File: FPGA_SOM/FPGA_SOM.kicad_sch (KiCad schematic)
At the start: 95 parts, among them J1 Conn_02x06_Top_Bottom, J1 USB_C_Receptacle_USB2.0, J10 Conn_01x06, J2 Conn_02x05_Counter_Clockwise, J5 Conn_01x02, J6 Conn_01x06, J9 RJ45_Bel_SI-60062-F, SW1 SW_Push, U1 ICE40UP5K-SG48ITR, U101 W25Q128JVSIQ, U2 AP2127N-3.3, U3 AP2127N-1.2, U6 LAN8720A, X101 SX2M20.000B10F20TNN, Y1 25 MHz

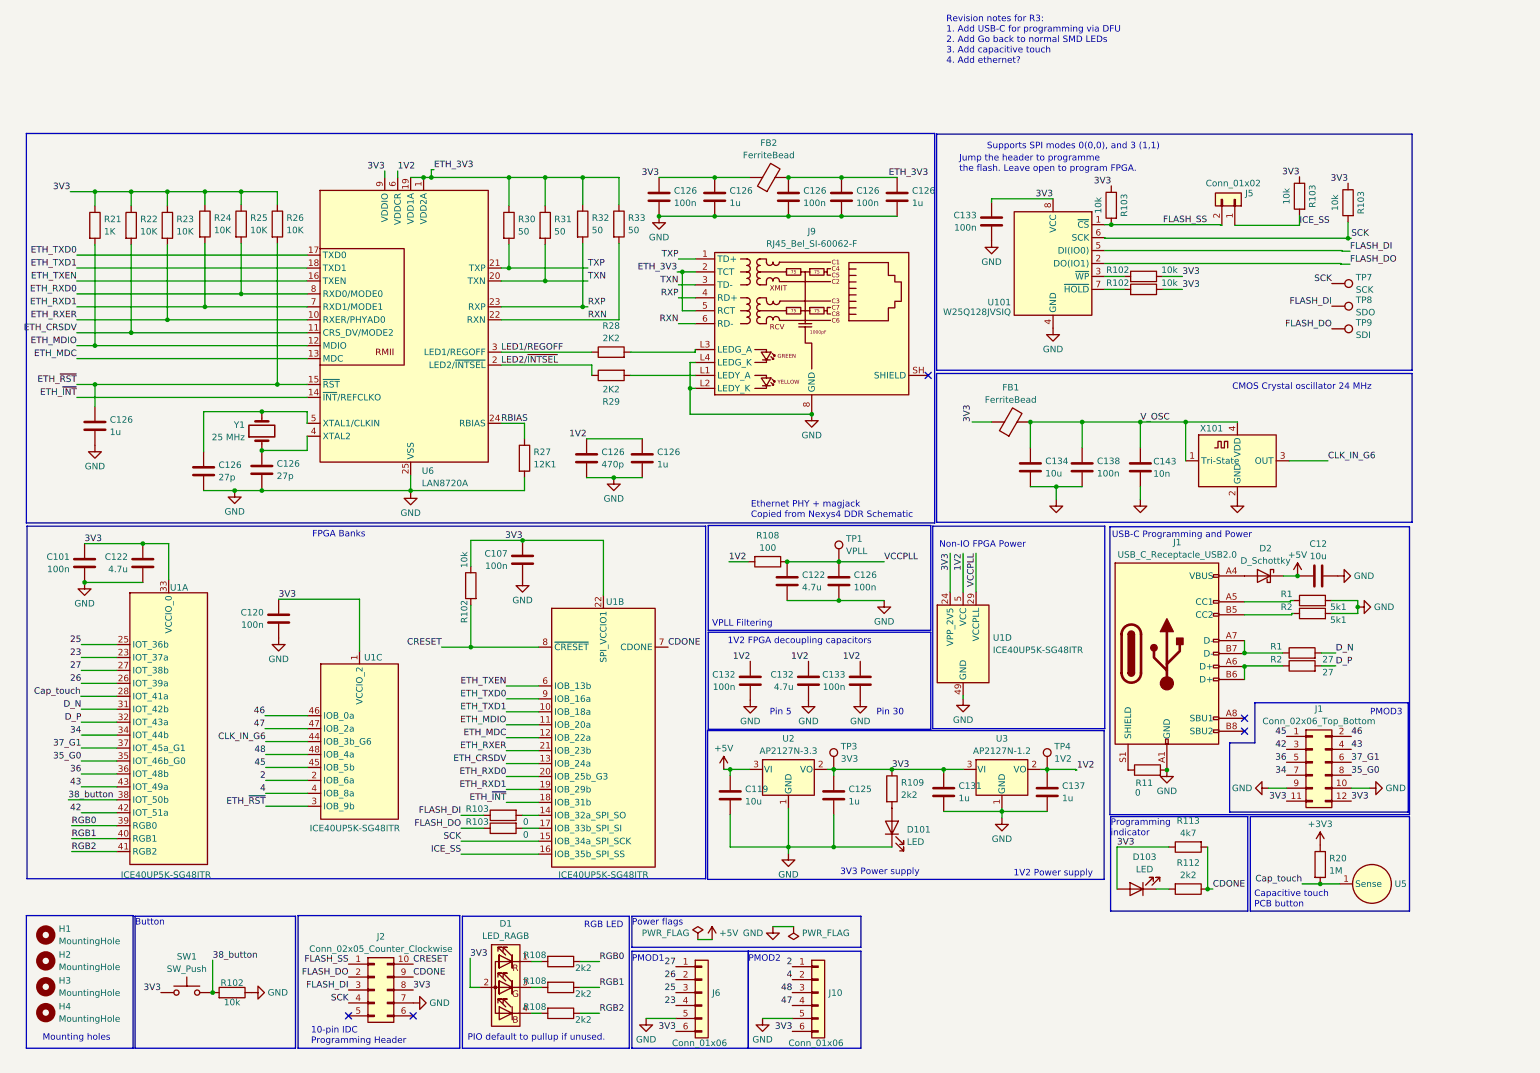
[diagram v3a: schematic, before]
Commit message: V3. New form factor, many improvements.
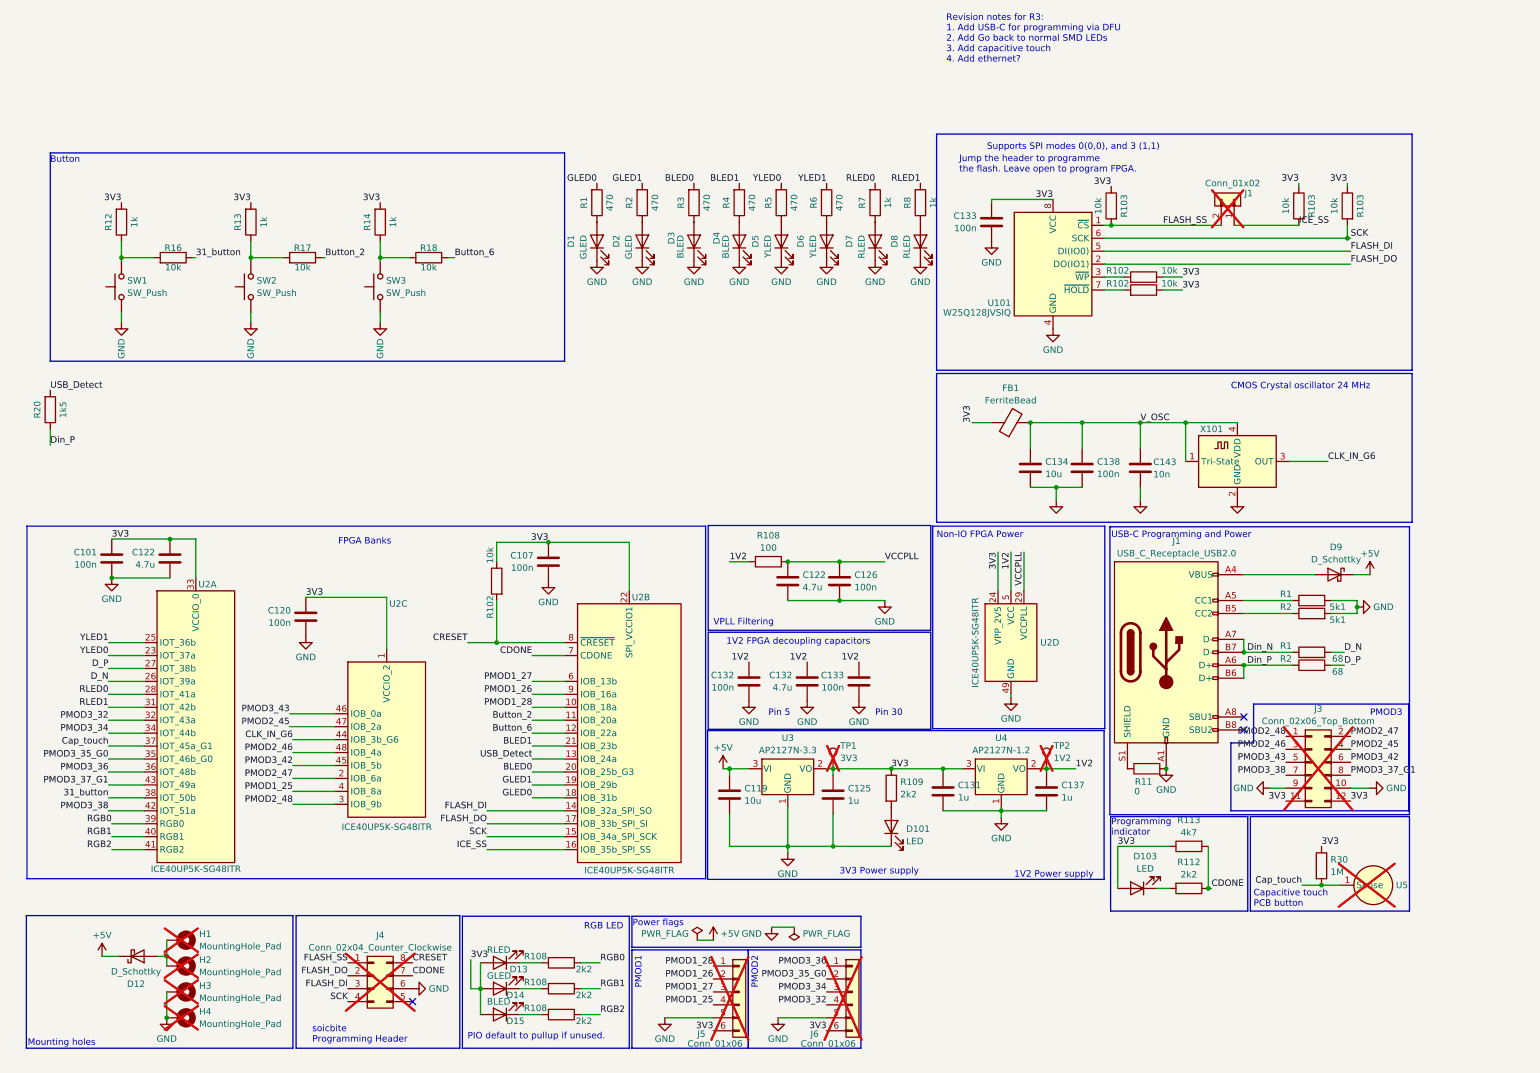
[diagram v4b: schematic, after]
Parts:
- removed C12: 10u, Capacitor_SMD:C_0603_1608Metric, symbol Device:C
- removed C126 (x2): 27p, Capacitor_SMD:C_0402_1005Metric, symbol Device:C
- removed C126 (x3): 100n, Capacitor_SMD:C_0402_1005Metric, symbol Device:C
- removed C126 (x4): 1u, Capacitor_SMD:C_0402_1005Metric, symbol Device:C
- removed C126: 470p, Capacitor_SMD:C_0402_1005Metric, symbol Device:C
- removed D1: LED_RAGB, LED_SMD:LED_SK6812_EC15_1.5x1.5mm, symbol Device:LED_RAGB
- removed FB2: FerriteBead, Resistor_SMD:R_0603_1608Metric, symbol Device:FerriteBead
- removed H1, H2, H3, H4: MountingHole, MountingHole:MountingHole_3.2mm_M3_DIN965_Pad, symbol Mechanical:MountingHole
- removed J10: Conn_01x06, Connector_PinHeader_2.54mm:PinHeader_1x06_P2.54mm_Horizontal, symbol Connector_Generic:Conn_01x06
- removed J2: Conn_02x05_Counter_Clockwise, Connector_PinHeader_2.54mm:PinHeader_2x05_P2.54mm_Vertical, symbol Connector_Generic:Conn_02x05_Counter_Clockwise
- removed J9: RJ45_Bel_SI-60062-F, Connector_RJ:RJ45_Bel_SI-60062-F, symbol Connector:RJ45_Bel_SI-60062-F
- removed R102: 10k, Resistor_SMD:R_0402_1005Metric, symbol Device:R
- removed R103 (x2): 0, Resistor_SMD:R_0402_1005Metric, symbol Device:R
- removed R21: 1K, Resistor_SMD:R_0402_1005Metric, symbol Device:R
- removed R22, R23, R24, R25, R26: 10K, Resistor_SMD:R_0402_1005Metric, symbol Device:R
- removed R27: 12K1, Resistor_SMD:R_0402_1005Metric, symbol Device:R
- removed R28, R29: 2K2, Resistor_SMD:R_0402_1005Metric, symbol Device:R
- removed R30, R31, R32, R33: 50, Resistor_SMD:R_0402_1005Metric, symbol Device:R
- removed TP1: VPLL, TestPoint:TestPoint_THTPad_D2.0mm_Drill1.0mm, symbol Connector:TestPoint
- removed TP7: SCK, TestPoint:TestPoint_THTPad_D2.0mm_Drill1.0mm, symbol Connector:TestPoint
- removed TP8: SDO, TestPoint:TestPoint_THTPad_D2.0mm_Drill1.0mm, symbol Connector:TestPoint
- removed TP9: SDI, TestPoint:TestPoint_THTPad_D2.0mm_Drill1.0mm, symbol Connector:TestPoint
- removed U6: LAN8720A, Package_DFN_QFN:VQFN-24-1EP_4x4mm_P0.5mm_EP2.5x2.5mm_ThermalVias, symbol Interface_Ethernet:LAN8720A
- removed Y1: 25 MHz, Crystal:Crystal_SMD_2520-4Pin_2.5x2.0mm, symbol Device:Crystal
- added D1, D14, D2: GLED, LED_SMD:LED_0805_2012Metric, symbol Device:LED
- added D12: D_Schottky, Diode_SMD:D_0603_1608Metric, symbol Device:D_Schottky
- added D13, D7, D8: RLED, LED_SMD:LED_0805_2012Metric, symbol Device:LED
- added D15, D3, D4: BLED, LED_SMD:LED_0805_2012Metric, symbol Device:LED
- added D5, D6: YLED, LED_SMD:LED_0805_2012Metric, symbol Device:LED
- added H1, H2, H3, H4: MountingHole_Pad, MountingHole:MountingHole_3.2mm_M3_ISO7380_Pad_TopBottom, symbol Mechanical:MountingHole_Pad
- added J4: Conn_02x04_Counter_Clockwise, ACustomFootprintLib:SOIC_clipProgSmall, symbol Connector_Generic:Conn_02x04_Counter_Clockwise
- added J5: Conn_01x06, Connector_PinHeader_2.54mm:PinHeader_1x06_P2.54mm_Horizontal, symbol Connector_Generic:Conn_01x06
- added R1, R2, R3, R4, R5, R6: 470, Resistor_SMD:R_0402_1005Metric, symbol Device:R
- added R12, R13, R14, R7, R8: 1k, Resistor_SMD:R_0402_1005Metric, symbol Device:R
- added R16, R17, R18: 10k, Resistor_SMD:R_0402_1005Metric, symbol Device:R
- added R20: 1k5, Resistor_SMD:R_0402_1005Metric, symbol Device:R
- added SW2, SW3: SW_Push, Button_Switch_SMD:SW_SPST_PTS810, symbol Switch:SW_Push
- C101, C107, C120, C126, C132, C133, C138: LCSC (none) -> CL05B104KO5NNNC; LCSC Part # C14663 -> C1525
- C119, C134: LCSC (none) -> CL10A106KP8NNNC; LCSC Part # C96446 -> C19702
- C122, C132: LCSC (none) -> CL10A475KO8NNNC
- C125, C131, C137: LCSC (none) -> CL05A105KA5NQNC; LCSC Part # C15849 -> C52923
- C143: LCSC (none) -> CL05B103KB5NNNC; LCSC Part # C57112 -> C15195
- D101: LCSC (none) -> KT-0603W; LCSC Part # (none) -> C2290; Price 0.2853 -> (none)
- D103: LCSC (none) -> KT-0603W; LCSC Part # (none) -> C2290; Price 0.5157 -> (none)
- D9: renamed from D2; LCSC (none) -> Comchip CDBVRL140-HF; LCSC Part # (none) -> C3758192
- FB1: LCSC (none) -> GZ1608D601TF
- J1: renamed from J5; LCSC (none) -> N/A; LCSC Part # (none) -> N/A; now not fitted
- J1: JLC Link https://jlcpcb.com/partdetail/gswitch-GT_USB7004N/C2848971 -> (none); JLC Part Number C2848971 -> (none); LCSC (none) -> GT-USB-7004N; LCSC Part # (none) -> C2848971
- J3: renamed from J1; LCSC (none) -> N/A; LCSC Part # (none) -> N/A; now not fitted
- J6: LCSC (none) -> N/A; LCSC Part # (none) -> N/A; now not fitted
- R1, R2: JLC Link https://jlcpcb.com/partdetail/26648-0402WGF5101TCE/C25905 -> (none); JLC Part Number C25905 -> (none); LCSC (none) -> 0402WGF5101TCE; LCSC Part # (none) -> C25905
- R1, R2: value 27 -> 68; JLC Link https://jlcpcb.com/partdetail/26648-0402WGF5101TCE/C25905 -> (none); JLC Part Number C25905 -> (none); LCSC (none) -> 0402WGF680JTCE; LCSC Part # (none) -> C25131
- R102, R103: LCSC (none) -> 0402WGF1002TCE; LCSC Part # C25804 -> C25744
- R108: LCSC (none) -> 0402WGF1000TCE; LCSC Part # C22775 -> C25076
- R108, R109, R112: LCSC (none) -> 0402WGF2201TCE; LCSC Part # C4190 -> C25879
- R11: JLC Link https://jlcpcb.com/partdetail/26628-0402WGF2701TCE/C25885 -> (none); JLC Part Number C17168 -> (none); LCSC (none) -> 0402WGF0000TCE; LCSC Part # (none) -> C17168
- R113: LCSC (none) -> 0402WGF4701TCE; LCSC Part # C23162 -> C25900
- R30: renamed from R20; LCSC (none) -> 0603WAF1004T5E; LCSC Part # (none) -> C22935
- SW1: footprint Button_Switch_THT:SW_PUSH_6mm -> Button_Switch_SMD:SW_SPST_PTS810; LCSC (none) -> TSA016A2518C; LCSC Part # (none) -> C2888430
- TP1: renamed from TP3; footprint TestPoint:TestPoint_THTPad_D2.0mm_Drill1.0mm -> TestPoint:TestPoint_Pad_D1.0mm; LCSC (none) -> N/A; LCSC Part # (none) -> N/A; now not fitted
- TP2: renamed from TP4; footprint TestPoint:TestPoint_THTPad_D2.0mm_Drill1.0mm -> TestPoint:TestPoint_Pad_D1.0mm; LCSC (none) -> N/A; LCSC Part # (none) -> N/A; now not fitted
- U101: LCSC (none) -> W25Q128JVSIQ; Price 0.8395 -> (none)
- U2: renamed from U1; LCSC (none) -> ICE40UP5K-SG48ITR
- U3: renamed from U2; DigiKey https://www.digikey.co.nz/en/products/detail/diodes-incorpo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 -> (none); LCSC (none) -> AP2127N-3.3TRG1; LCSC Part # (none) -> C176954
- U4: renamed from U3; DigiKey https://www.digikey.co.nz/en/products/detail/diodes-incorpo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 -> (none); LCSC (none) -> DS8561-12SS3; LCSC Part # (none) -> C18199516
- U5: now not fitted
- X101: value SX2M20.000B10F20TNN -> SX2M36.000B10F20TNN; LCSC (none) -> ASDM1-24.000MHZ-LC-T; LCSC Part # C7431315 -> C1987235; Price 3.024 -> (none)
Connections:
- net +3V3 is gone; now on net 3V3: R30.1
- net 47 is gone; now on net PMOD2_45: U2.47 (IOB_2a)
- net 48 is gone; now on net PMOD2_46: U2.48 (IOB_4a)
- net ETH_~{RST} is gone; now on net PMOD2_48: U2.3 (IOB_9b)
- net +5V: now also D12.1 (K)
- net 3V3: now also D13.2 (A), D14.2 (A), D15.2 (A), J5.6 (Pin_6), R12.2, R13.2, R14.2; no longer SW1.1
- net CDONE: now also J4.7 (Pin_7)
- net CRESET: now also J4.8 (Pin_8)
- net Cap_touch: now also U2.37 (IOT_45a_G1); no longer U2.28 (IOT_41a)
- net D_N: now also U2.26 (IOT_39a); no longer U2.31 (IOT_42b)
- net D_P: now also U2.27 (IOT_38b); no longer U2.32 (IOT_43a)
- net FLASH_DI: now also U2.14 (IOB_32a_SPI_SO), J4.3 (Pin_3)
- net FLASH_DO: now also U2.17 (IOB_33b_SPI_SI), J4.2 (Pin_2)
- net FLASH_SS: now also J4.1 (Pin_1)
- net GND: now also SW1.1, D1.1 (K), D2.1 (K), D3.1 (K), D4.1 (K), D5.1 (K), D6.1 (K), D7.1 (K), D8.1 (K), H3.1, H4.1, J4.6 (Pin_6), J5.5 (Pin_5), SW2.1, SW3.1
- net SCK: now also J4.4 (Pin_4)
- net at R108.2: now also D15.1 (K)
- net Din_P: now reaches J1.A6 (D+), J1.B6 (D+), R2.1
- net Din_P: now also R20.1
- net at R108.2: now also D13.1 (K)
- net at R108.2: now also D14.1 (K)
- net Din_N: now reaches J1.A7 (D-), J1.B7 (D-), R1.1
- net 2 renamed PMOD2_47
- net PMOD2_47: now also J3.2 (Pin_2)
- net 23 renamed PMOD3_32
- net PMOD3_32: now also U2.32 (IOT_43a); no longer U2.23 (IOT_37a)
- net 25 renamed PMOD3_34
- net PMOD3_34: now also U2.34 (IOT_44b); no longer U2.25 (IOT_36b)
- net 26 renamed PMOD3_35_G0
- net PMOD3_35_G0: now also U2.35 (IOT_46b_G0); no longer U2.26 (IOT_39a)
- net 27 renamed PMOD3_36
- net PMOD3_36: now also U2.36 (IOT_48b); no longer U2.27 (IOT_38b)
- net 34 renamed PMOD3_38
- net PMOD3_38: now also U2.42 (IOT_51a); no longer U2.34 (IOT_44b)
- net 35_G0 renamed PMOD3_37_G1
- net PMOD3_37_G1: now also U2.43 (IOT_49a); no longer U2.35 (IOT_46b_G0)
- net 36 renamed PMOD3_43
- net PMOD3_43: now also U2.46 (IOB_0a); no longer U2.36 (IOT_48b)
- net 37_G1 renamed PMOD3_42
- net PMOD3_42: now also U2.45 (IOB_5b); no longer U2.37 (IOT_45a_G1)
- net 38_button: no longer names the net of SW1.2
- net 38_button: now also R12.1, R16.2; no longer U2.38 (IOT_50b)
- net 4 renamed PMOD1_25
- net PMOD1_25: now also J5.4 (Pin_4)
- net 42 renamed PMOD2_46
- net PMOD2_46: no longer U2.42 (IOT_51a)
- net 43 renamed PMOD2_45
- net PMOD2_45: no longer U2.43 (IOT_49a)
- net 45 renamed PMOD2_48
- net PMOD2_48: no longer U2.45 (IOB_5b)
- removed net 46: J3.2 (Pin_2), U2.46 (IOB_0a)
- net ETH_CRSDV renamed USB_Detect
- net USB_Detect: now also R20.2
- net ETH_MDC renamed Button_6
- net Button_6: now also R18.1
- net ETH_MDIO renamed Button_2
- net Button_2: now also R17.1
- net ETH_RXD0 renamed BLED0
- net BLED0: now also R3.2
- net ETH_RXD1 renamed GLED1
- net GLED1: now also R2.2
- net ETH_RXER renamed BLED1
- net BLED1: now also R4.2
- net ETH_TXD0 renamed PMOD1_26
- net PMOD1_26: now also J5.2 (Pin_2)
- net ETH_TXD1 renamed PMOD1_28
- net PMOD1_28: now also J5.1 (Pin_1)
- net ETH_TXEN renamed PMOD1_27
- net PMOD1_27: now also J5.3 (Pin_3)
- net ETH_~{INT} renamed GLED0
- net GLED0: now also R1.2
- new net: D1.2 (A), R1.1
- new net: D6.2 (A), R6.1
- new net: D12.2 (A), H1.1, H2.1
- new net: R13.1, R17.2, SW2.2
- new net: D8.2 (A), R8.1
- new net: D5.2 (A), R5.1
- new net: R14.1, R18.2, SW3.2
- new net: D7.2 (A), R7.1
- new net: D2.2 (A), R2.1
- new net: D4.2 (A), R4.1
- new net: D3.2 (A), R3.1
- new net 31_button: R16.1, U2.38 (IOT_50b)
- new net RLED0: R7.2, U2.28 (IOT_41a)
- new net RLED1: R8.2, U2.31 (IOT_42b)
- new net YLED0: R5.2, U2.23 (IOT_37a)
- new net YLED1: R6.2, U2.25 (IOT_36b)
- no-connect marks 5 -> 3
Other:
- note added: "soicbite Programming Header"
- note removed: "10-pin IDC Programming Header"
- note removed: "Ethernet PHY + magjack Copied from Nexys4 DDR Schematic"
- moved on the sheet: C101, C107, C120, C122, D9, R1, R102, R103, R2, U2A, U2B, U2C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

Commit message: Final version 3 sent for assembly.
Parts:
- R1, R2: value 68 -> 22; LCSC 0402WGF680JTCE -> 0402WGF220JTCE; LCSC Part # C25131 -> C25092
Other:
- moved on the sheet: R1, R2
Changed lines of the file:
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@@
 	)
 	(junction
+		(at 251.46 117.475)
+		(diameter 0)
+		(color 0 0 0 0)
+	)
+	(junction
 		(at 172.085 96.52)
 		(diameter 0)
@@
 	)
 	(junction
-		(at 251.46 116.84)
-		(diameter 0)
-		(color 0 0 0 0)
-	)
-	(junction
 		(at 31.115 36.83)
 		(diameter 0)
@@
 	(wire
 		(pts
-			(xy 251.46 116.84) (xy 251.46 119.38)
+			(xy 251.46 116.84) (xy 251.46 117.475)
 		)
 		(stroke
@@
 	(wire
 		(pts
+			(xy 251.46 114.935) (xy 265.43 114.935)
+		)
+		(stroke
+			(width 0)
+			(type default)
+		)
+	)
+	(wire
+		(pts
 			(xy 144.145 170.815) (xy 147.32 170.815)
 		)
@@
 	(wire
 		(pts
-			(xy 251.46 114.3) (xy 260.985 114.3)
+			(xy 169.545 137.16) (xy 170.815 137.16)
 		)
 		(stroke
@@
 	(wire
 		(pts
-			(xy 169.545 137.16) (xy 170.815 137.16)
+			(xy 64.77 136.525) (xy 73.025 136.525)
 		)
 		(stroke
@@
 	(wire
 		(pts
-			(xy 64.77 136.525) (xy 73.025 136.525)
+			(xy 251.46 117.475) (xy 265.43 117.475)
 		)
 		(stroke
@@
 	(wire
 		(pts
-			(xy 271.145 114.3) (xy 268.605 114.3)
+			(xy 275.59 114.935) (xy 273.05 114.935)
 		)
 		(stroke
@@
 	(wire
 		(pts
+			(xy 251.46 114.935) (xy 251.46 114.3)
+		)
+		(stroke
+			(width 0)
+			(type default)
+		)
+	)
+	(wire
+		(pts
 			(xy 231.14 74.295) (xy 231.14 69.215)
 		)
@@
 	(wire
 		(pts
-			(xy 271.145 116.84) (xy 268.605 116.84)
+			(xy 275.59 117.475) (xy 273.05 117.475)
 		)
 		(stroke
@@
 	(wire
 		(pts
+			(xy 251.46 117.475) (xy 251.46 119.38)
+		)
+		(stroke
+			(width 0)
+			(type default)
+		)
+	)
+	(wire
+		(pts
 			(xy 45.72 92.075) (xy 45.72 99.695)
 		)
@@
 	(wire
 		(pts
-			(xy 260.985 116.84) (xy 251.46 116.84)
-		)
-		(stroke
-			(width 0)
-			(type default)
-		)
-	)
-	(wire
-		(pts
 			(xy 101.6 180.34) (xy 99.695 180.34)
 		)
@@
 	)
 	(label "Din_P"
-		(at 252.095 116.84 0)
+		(at 256.54 117.475 0)
 		(fields_autoplaced yes)
 		(effects
@@
 	)
 	(label "D_N"
-		(at 271.145 114.3 0)
+		(at 275.59 114.935 0)
 		(fields_autoplaced yes)
 		(effects
@@
 	)
 	(label "Din_N"
-		(at 252.095 114.3 0)
+		(at 256.54 114.935 0)
 		(fields_autoplaced yes)
 		(effects
@@
 	)
 	(label "D_P"
-		(at 271.145 116.84 0)
+		(at 275.59 117.475 0)
 		(fields_autoplaced yes)
 		(effects
@@
 	(symbol
 		(lib_id "Device:R")
-		(at 264.795 116.84 90)
+		(at 269.24 117.475 90)
 		(unit 1)
 		(exclude_from_sim no)
@@
 		(dnp no)
 		(property "Reference" "R2"
-			(at 259.715 115.57 90)
+			(at 264.16 116.205 90)
 			(effects
 				(font
@@
 			)
 		)
-		(property "Value" "68"
-			(at 269.875 118.11 90)
+		(property "Value" "22"
+			(at 274.32 118.745 90)
 			(effects
 				(font
@@
 		)
 		(property "Footprint" "Resistor_SMD:R_0402_1005Metric"
-			(at 264.795 118.618 90)
+			(at 269.24 119.253 90)
 			(effects
 				(font
@@
 		)
 		(property "Datasheet" "https://wmsc.lcsc.com/wmsc/upload/file/pdf/v2/lcsc/2206010045_UNI-ROYAL-Uniroyal-Elec-0402WGF5101TCE_C25905.pdf"
-			(at 264.795 116.84 0)
+			(at 269.24 117.475 0)
 			(effects
 				(font
@@
 		)
 		(property "Description" ""
-			(at 264.795 116.84 0)
+			(at 269.24 117.475 0)
 			(effects
 				(font
@@
 			)
 		)
-		(property "LCSC" "0402WGF680JTCE"
-			(at 264.795 116.84 0)
+		(property "LCSC" "0402WGF220JTCE"
+			(at 269.24 117.475 0)
 			(effects
 				(font
@@
 			)
 		)
-		(property "LCSC Part #" "C25131"
-			(at 264.795 116.84 0)
+		(property "LCSC Part #" "C25092"
+			(at 269.24 117.475 0)
 			(effects
 				(font
@@
 	(symbol
 		(lib_id "Device:R")
-		(at 264.795 114.3 90)
+		(at 269.24 114.935 90)
 		(unit 1)
 		(exclude_from_sim no)
@@
 		(dnp no)
 		(property "Reference" "R1"
-			(at 259.715 113.03 90)
+			(at 264.16 113.665 90)
 			(effects
 				(font
@@
 			)
 		)
-		(property "Value" "68"
-			(at 269.875 115.57 90)
+		(property "Value" "22"
+			(at 274.32 116.205 90)
 			(effects
 				(font
@@
 		)
 		(property "Footprint" "Resistor_SMD:R_0402_1005Metric"
-			(at 264.795 116.078 90)
+			(at 269.24 116.713 90)
 			(effects
 				(font
@@
 		)
 		(property "Datasheet" "https://wmsc.lcsc.com/wmsc/upload/file/pdf/v2/lcsc/2206010045_UNI-ROYAL-Uniroyal-Elec-0402WGF5101TCE_C25905.pdf"
-			(at 264.795 114.3 0)
+			(at 269.24 114.935 0)
 			(effects
 				(font
@@
 		)
 		(property "Description" ""
-			(at 264.795 114.3 0)
+			(at 269.24 114.935 0)
 			(effects
 				(font
@@
 			)
 		)
-		(property "LCSC" "0402WGF680JTCE"
-			(at 264.795 114.3 0)
+		(property "LCSC" "0402WGF220JTCE"
+			(at 269.24 114.935 0)
 			(effects
 				(font
@@
 			)
 		)
-		(property "LCSC Part #" "C25131"
-			(at 264.795 114.3 0)
+		(property "LCSC Part #" "C25092"
+			(at 269.24 114.935 0)
 			(effects
 				(font
